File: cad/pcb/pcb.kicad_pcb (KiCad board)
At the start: 4 copper layers, 60 x 60 mm, 108 parts, among them X1 USB_C_Receptacle_USB2.0, X2 Bat-Conn, X3 NTC, X4 SWD-Conn, X5 UART_Conn, Y1 32MHz, Y2 32.768k

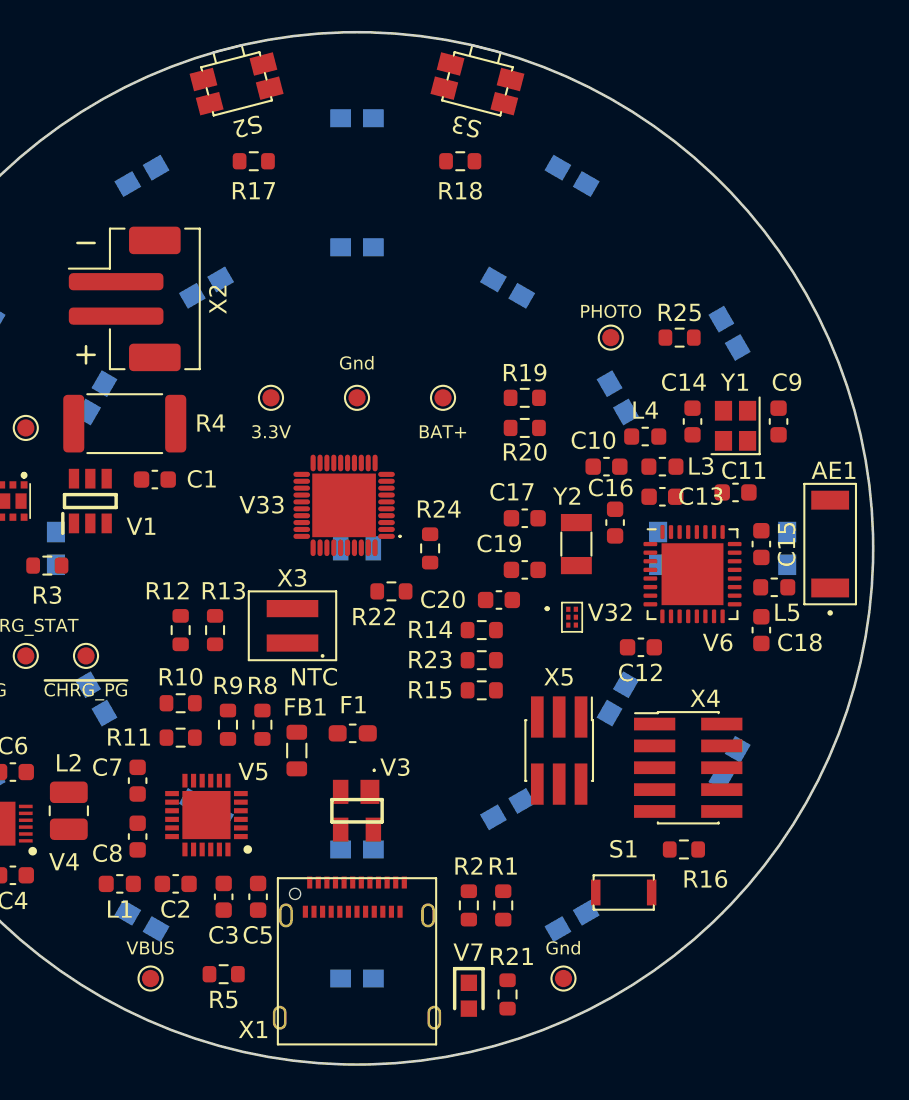
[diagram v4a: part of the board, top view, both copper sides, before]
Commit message: route mcu section
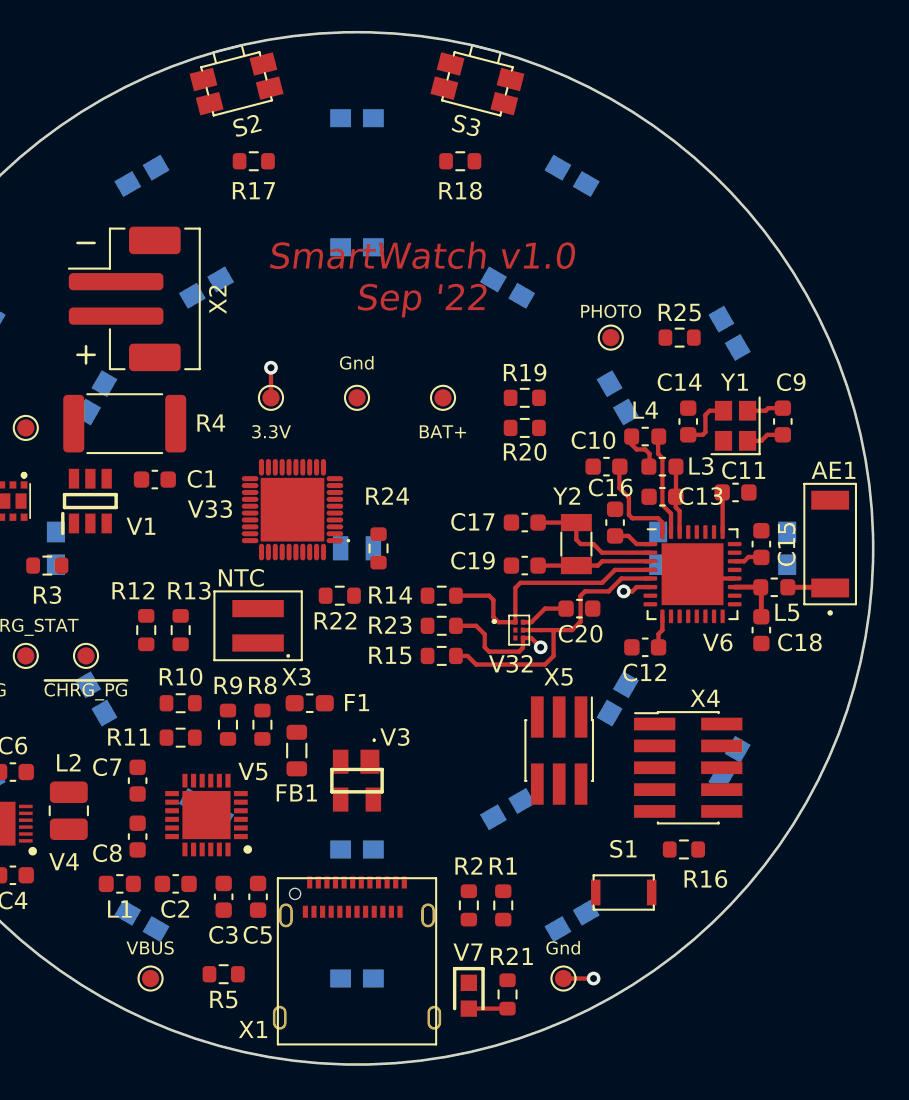
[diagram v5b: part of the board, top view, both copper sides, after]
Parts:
- moved C20 4.70 mm to (162.9, 103.5), turned to 0 degrees
- moved V32 3.17 mm to (159.4, 104.8)
- moved R14 3.07 mm to (154.9, 102.8)
- moved R15 3.07 mm to (154.9, 106.2)
- moved R23 3.07 mm to (154.9, 104.5)
- moved F1 3.05 mm to (147.2, 109.0)
- moved R22 3.01 mm to (149.0, 102.8)
- moved V33 3.01 mm to (146.2, 97.8)
- moved R24 3.00 mm to (151.2, 100.0)
- moved R12 2.00 mm to (137.8, 104.8)
- moved R13 2.00 mm to (139.8, 104.8)
- moved X3 2.00 mm to (144.2, 104.5)
- moved V3 1.75 mm to (150.0, 113.5)
- moved C12 0.25 mm to (166.8, 105.8)
- moved C14 0.25 mm to (169.2, 92.6)
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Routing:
- net SDA: track 0.00 -> 17.1 mm
- net SCL: track 0.00 -> 15.0 mm
- net 3.3V: track 0.00 -> 14.5 mm, vias 0 -> 1
- net GYRO_INT: track 0.00 -> 8.52 mm, vias 0 -> 2
- net LSE1: track 0.00 -> 7.84 mm
- net LSE2: track 0.00 -> 6.63 mm
- net BAT_PROT-: track 0.00 -> 6.42 mm, vias 0 -> 1
- net /MCU/DCC: track 0.00 -> 5.88 mm
- net /MCU/DEC4: track 0.00 -> 3.90 mm
- net /MCU/ANT_IN: track 0.00 -> 3.25 mm
- net HSE2: track 0.00 -> 3.22 mm
- net Net-(L3-Pad1): track 0.00 -> 2.49 mm
- net /MCU/ANT_TP: track 0.00 -> 2.48 mm
- net Net-(R21-Pad2): track 0.00 -> 2.25 mm
- net /MCU/DEC1: track 0.00 -> 2.25 mm
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- added copper zone on In2.Cu, net 3.3V
- added copper zone on In1.Cu, net BAT_PROT-
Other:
- board text added: "SmartWatch v1.0 Sep '22"

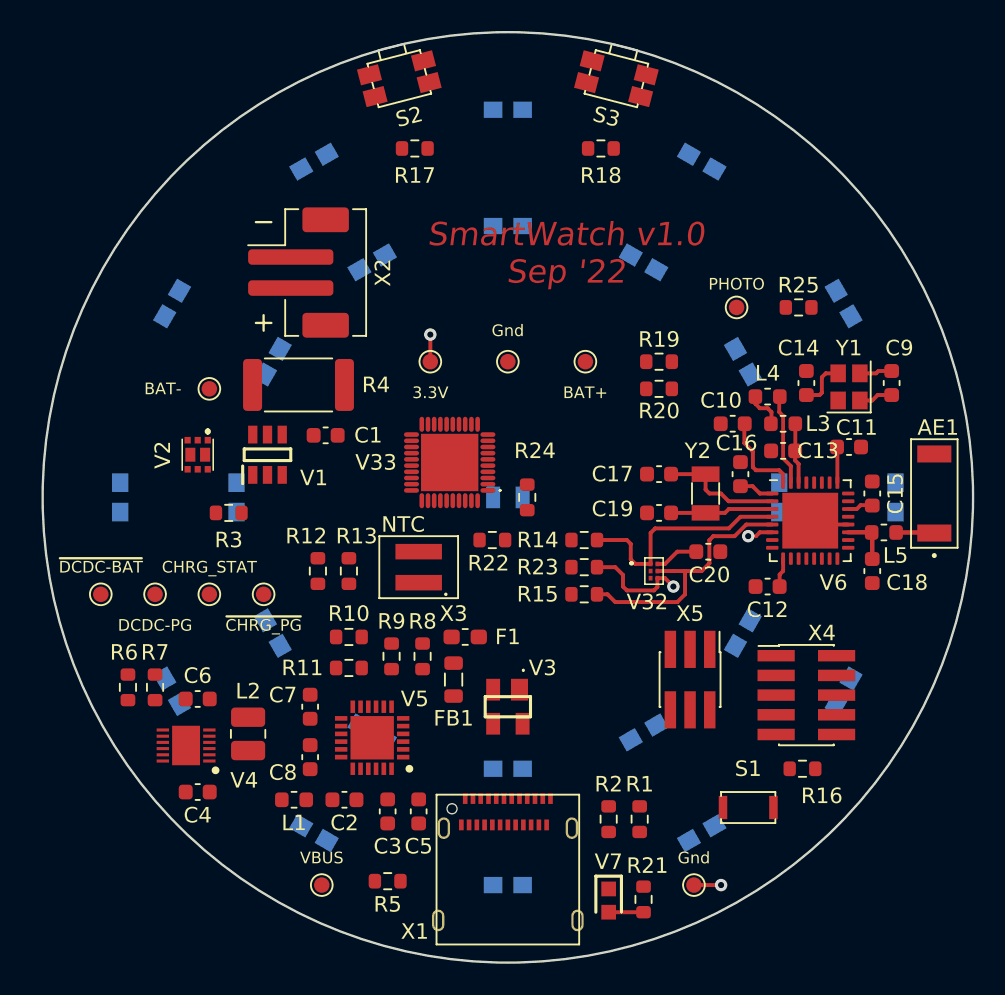
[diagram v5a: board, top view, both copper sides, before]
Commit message: add 3d models for pcb layout
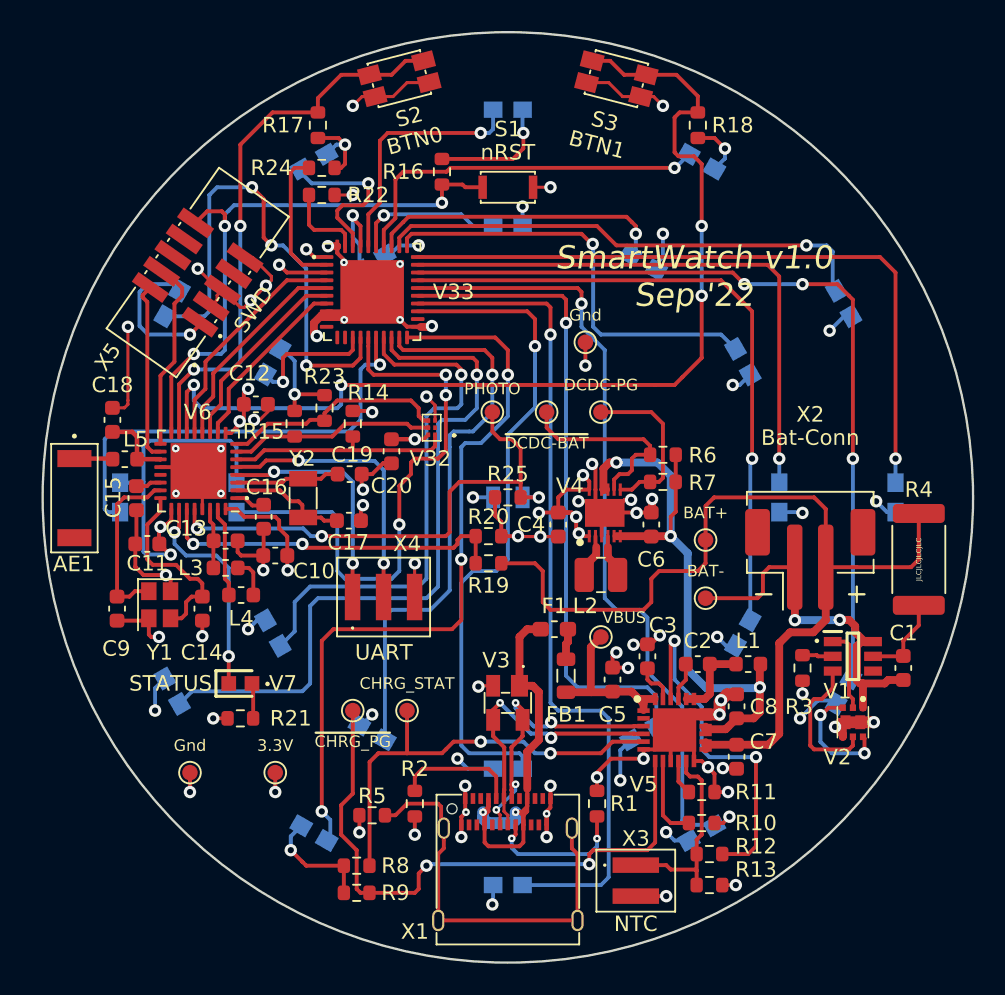
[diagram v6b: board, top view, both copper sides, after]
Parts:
- V33: footprint IO Expander:PCA9957HNMP -> Package_DFN_QFN:HVQFN-40-1EP_6x6mm_P0.5mm_EP4.1x4.1mm
- X4: value SWD-Conn -> UART; footprint Connector_PinHeader_1.27mm:PinHeader_2x05_P1.27mm_Vertical_SMD -> myLib:PinHeader_P2mm_1x03_SMD
- X5: value UART_Conn -> SWD; footprint Connector_PinHeader_1.27mm:PinHeader_2x03_P1.27mm_Vertical_SMD -> myLib:PinHeader_2x05_P1.27mm_Vertical_SMD
- moved AE1 55.5 mm to (122.0, 100.0), turned to -90 degrees
- moved C9 52.0 mm to (124.8, 107.2), turned to 90 degrees
- moved C18 50.0 mm to (124.5, 95.0), turned to 90 degrees
- moved L5 49.2 mm to (125.3, 97.5), turned to 0 degrees
- moved C15 47.5 mm to (126.0, 100.0), turned to -90 degrees
- moved Y1 46.6 mm to (127.5, 106.9), turned to -90 degrees
- moved C11 45.7 mm to (126.8, 103.0), turned to 180 degrees
- moved V2 45.6 mm to (172.2, 114.5)
- moved R16 45.0 mm to (145.8, 79.0), turned to -90 degrees
- moved S1 42.9 mm to (150.0, 80.0), turned to 180 degrees
- moved C14 41.6 mm to (130.3, 107.2), turned to 90 degrees
- moved R4 41.6 mm to (176.5, 104.0), turned to 90 degrees
- moved X5 41.2 mm to (130.0, 85.5), turned to 55 degrees
- moved C1 40.2 mm to (175.5, 111.0), turned to -90 degrees
- moved V1 39.9 mm to (172.2, 110.2), turned to 0 degrees
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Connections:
- V33 pad 13: Ring0_0 -> Ring1_2
- V33 pad 14: Ring1_0 -> Ring0_2
- V33 pad 15: Ring0_1 -> Ring1_3
- V33 pad 16: Ring1_1 -> Ring0_3
- V33 pad 17: Ring0_2 -> Ring1_4
- V33 pad 18: Ring1_2 -> Ring0_4
- V33 pad 19: Ring0_3 -> Ring1_5
- V33 pad 20: Ring1_3 -> Ring0_5
- V33 pad 23: Ring0_4 -> Ring1_6
- V33 pad 24: Ring1_4 -> Ring0_6
- V33 pad 25: Ring0_5 -> Ring1_7
- V33 pad 26: Ring1_5 -> Ring0_7
- V33 pad 27: Ring0_6 -> Ring1_8
- V33 pad 28: Ring1_6 -> Ring0_8
- V33 pad 29: Ring0_7 -> Ring1_9
- V33 pad 30: Ring1_7 -> Ring0_9
- V33 pad 31: Ring0_8 -> Ring1_10
- V33 pad 32: Ring1_8 -> Ring0_10
- V33 pad 33: Ring0_9 -> Ring1_11
- V33 pad 34: Ring1_9 -> Ring0_11
- V33 pad 35: Ring0_10 -> Ring1_0
- V33 pad 36: Ring1_10 -> Ring0_0
- V33 pad 37: Ring0_11 -> Ring1_1
- V33 pad 38: Ring1_11 -> Ring0_1
- V6 pad 14: DBG_LED -> BTN1
- V6 pad 26: BTN1 -> DBG_LED
- V6 pad 4: SCL -> TXD
- V6 pad 5: SDA -> RXD
- V6 pad 6: GYRO_INT -> SCL
- V6 pad 7: TXD -> SDA
- V6 pad 8: RXD -> GYRO_INT
- X4 pad 1: 3.3V -> TXD
- X4 pad 2: SWDIO -> RXD
- X5 pad 1: NRST -> 3.3V
- X5 pad 2: 3.3V -> SWDIO
- X5 pad 3: RXD -> BAT_PROT-
- X5 pad 4: BAT_PROT- -> SWDCLK
- X5 pad 5: TXD -> BAT_PROT-
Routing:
- net BAT_PROT-: track 6.42 -> 151.2 mm, vias 1 -> 63
- net 3.3V: track 14.5 -> 127.5 mm, vias 1 -> 38
- net BTN1: track 0.00 -> 66.6 mm, vias 0 -> 4
- net BAT_PROT+: track 0.00 -> 61.0 mm
- net Ring0_6: track 0.00 -> 54.3 mm, vias 0 -> 1
- net Ring0_8: track 0.00 -> 53.3 mm, vias 0 -> 3
- net Ring0_7: track 0.00 -> 50.5 mm, vias 0 -> 1
- net Ring0_5: track 0.00 -> 48.8 mm, vias 0 -> 3
- net Ring0_4: track 0.00 -> 45.8 mm, vias 0 -> 1
- net Ring0_9: track 0.00 -> 44.8 mm, vias 0 -> 1
- net Ring1_6: track 0.00 -> 43.2 mm, vias 0 -> 1
- net Ring1_8: track 0.00 -> 42.4 mm, vias 0 -> 1
- net Ring1_7: track 0.00 -> 42.1 mm, vias 0 -> 1
- net CHRG_OUT: track 0.00 -> 40.8 mm, vias 0 -> 3
- net /Power/~{CHRG_PG}: track 0.00 -> 39.1 mm, vias 0 -> 2
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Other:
- board text added: "JLCJLCJLCJLC"
- board text added: "STATUS"
